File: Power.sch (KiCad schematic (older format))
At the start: 0 parts

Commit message: Added Power Module outline
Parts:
- added C? (x2): C, ~, symbol C
- added F? (x4): FUSE, ~, symbol FUSE
- added L? (x2): INDUCTOR, ~, symbol INDUCTOR
- added P?: CONN_12X2, symbol CONN_12X2
- added R?: R, ~, symbol R
- added SW?: SWITCH_INV, ~, symbol SWITCH_INV
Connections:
- net labels added: +12P, +12V, +3.3V, +5V, -12P, -12V, GND
- wire segments 0 -> 37

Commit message: Fan Current module refactoring
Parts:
- removed F? (x4): FUSE, ~, symbol FUSE
- added TH? (x4): THERMISTOR, ~, symbol THERMISTOR
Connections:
- net labels added: +12C
- wire segments 37 -> 38
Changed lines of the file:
@@
 $Descr A4 11693 8268
 encoding utf-8
-Sheet 5 9
+Sheet 4 9
 Title ""
 Date "4 feb 2014"
@@
 	1    0    0    -1
 $EndComp
-$Comp
-L FUSE F?
-U 1 1 52EFD1CF
-P 3500 2850
-F 0 "F?" H 3600 2900 40  0000 C CNN
-F 1 "FUSE" H 3400 2800 40  0000 C CNN
-F 2 "~" H 3500 2850 60  0000 C CNN
-F 3 "~" H 3500 2850 60  0000 C CNN
-	1    3500 2850
-	1    0    0    -1
-$EndComp
-$Comp
-L FUSE F?
-U 1 1 52EFD1DC
-P 4300 3050
-F 0 "F?" H 4400 3100 40  0000 C CNN
-F 1 "FUSE" H 4200 3000 40  0000 C CNN
-F 2 "~" H 4300 3050 60  0000 C CNN
-F 3 "~" H 4300 3050 60  0000 C CNN
-	1    4300 3050
-	1    0    0    -1
-$EndComp
-$Comp
-L FUSE F?
-U 1 1 52EFD1E2
-P 5050 3250
-F 0 "F?" H 5150 3300 40  0000 C CNN
-F 1 "FUSE" H 4950 3200 40  0000 C CNN
-F 2 "~" H 5050 3250 60  0000 C CNN
-F 3 "~" H 5050 3250 60  0000 C CNN
-	1    5050 3250
-	1    0    0    -1
-$EndComp
-$Comp
-L FUSE F?
-U 1 1 52EFD1E8
-P 5950 3450
-F 0 "F?" H 6050 3500 40  0000 C CNN
-F 1 "FUSE" H 5850 3400 40  0000 C CNN
-F 2 "~" H 5950 3450 60  0000 C CNN
-F 3 "~" H 5950 3450 60  0000 C CNN
-	1    5950 3450
-	1    0    0    -1
-$EndComp
 Wire Wire Line
 	2950 2850 3250 2850
@@
 	9150 5100 9150 5250
 Connection ~ 8700 5100
+Wire Wire Line
+	3200 3250 3200 2400
+Connection ~ 3200 3250
+$Comp
+L +12C #PWR?
+U 1 1 52F156A2
+P 3200 2400
+F 0 "#PWR?" H 3200 2370 30  0001 C CNN
+F 1 "+12C" H 3200 2510 40  0000 C CNN
+F 2 "" H 3200 2400 60  0000 C CNN
+F 3 "" H 3200 2400 60  0000 C CNN
+	1    3200 2400
+	1    0    0    -1
+$EndComp
+$Comp
+L THERMISTOR TH?
+U 1 1 52F1698E
+P 3500 2850
+F 0 "TH?" V 3600 2900 50  0000 C CNN
+F 1 "THERMISTOR" V 3400 2850 50  0000 C CNN
+F 2 "~" H 3500 2850 60  0000 C CNN
+F 3 "~" H 3500 2850 60  0000 C CNN
+	1    3500 2850
+	0    -1   -1   0
+$EndComp
+$Comp
+L THERMISTOR TH?
+U 1 1 52F169A5
+P 4300 3050
+F 0 "TH?" V 4400 3100 50  0000 C CNN
+F 1 "THERMISTOR" V 4200 3050 50  0000 C CNN
+F 2 "~" H 4300 3050 60  0000 C CNN
+F 3 "~" H 4300 3050 60  0000 C CNN
+	1    4300 3050
+	0    -1   -1   0
+$EndComp
+$Comp
+L THERMISTOR TH?
+U 1 1 52F169AB
+P 5050 3250
+F 0 "TH?" V 5150 3300 50  0000 C CNN
+F 1 "THERMISTOR" V 4950 3250 50  0000 C CNN
+F 2 "~" H 5050 3250 60  0000 C CNN
+F 3 "~" H 5050 3250 60  0000 C CNN
+	1    5050 3250
+	0    -1   -1   0
+$EndComp
+$Comp
+L THERMISTOR TH?
+U 1 1 52F169B1
+P 5950 3450
+F 0 "TH?" V 6050 3500 50  0000 C CNN
+F 1 "THERMISTOR" V 5850 3450 50  0000 C CNN
+F 2 "~" H 5950 3450 60  0000 C CNN
+F 3 "~" H 5950 3450 60  0000 C CNN
+	1    5950 3450
+	0    -1   -1   0
+$EndComp
 $EndSCHEMATC

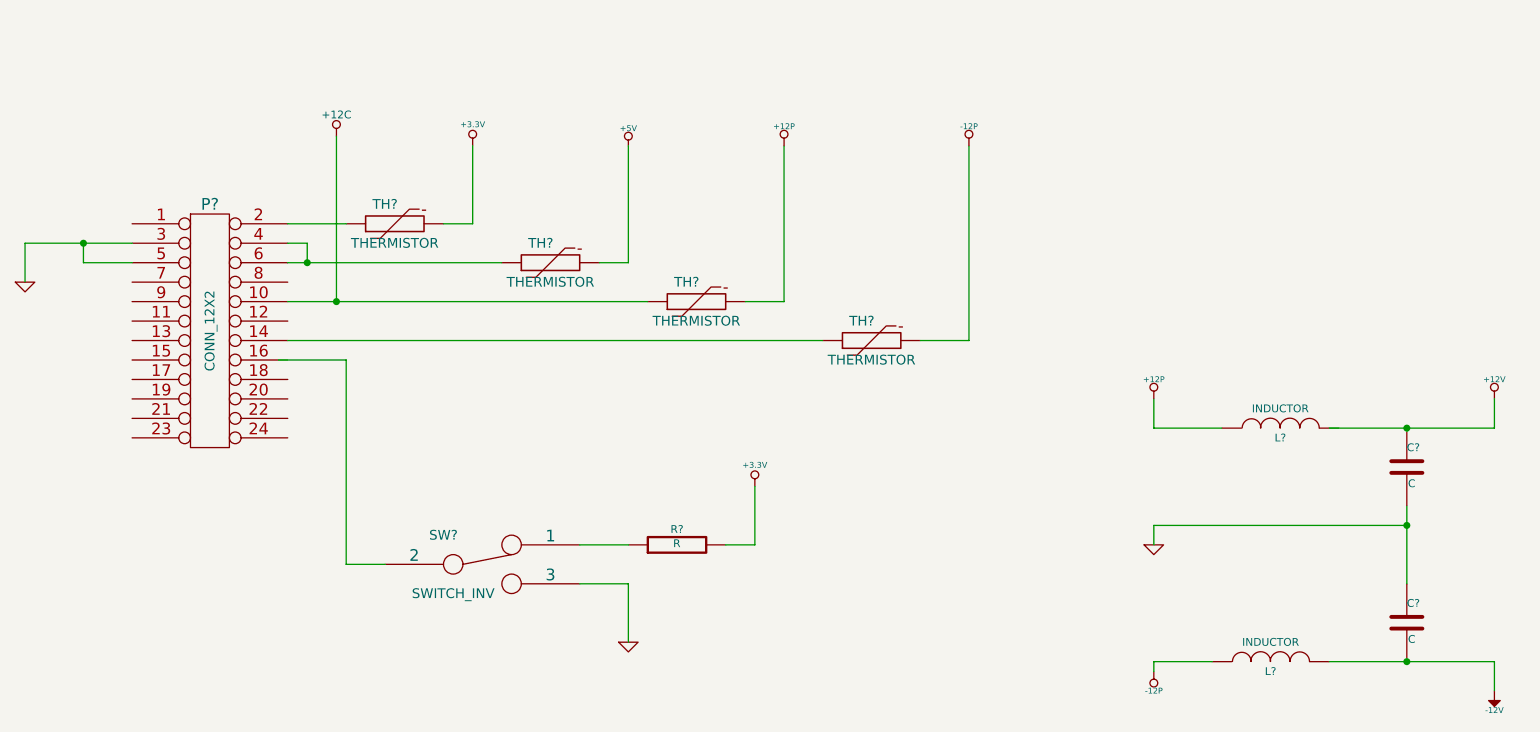
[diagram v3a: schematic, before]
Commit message: Begin Associating relay Module
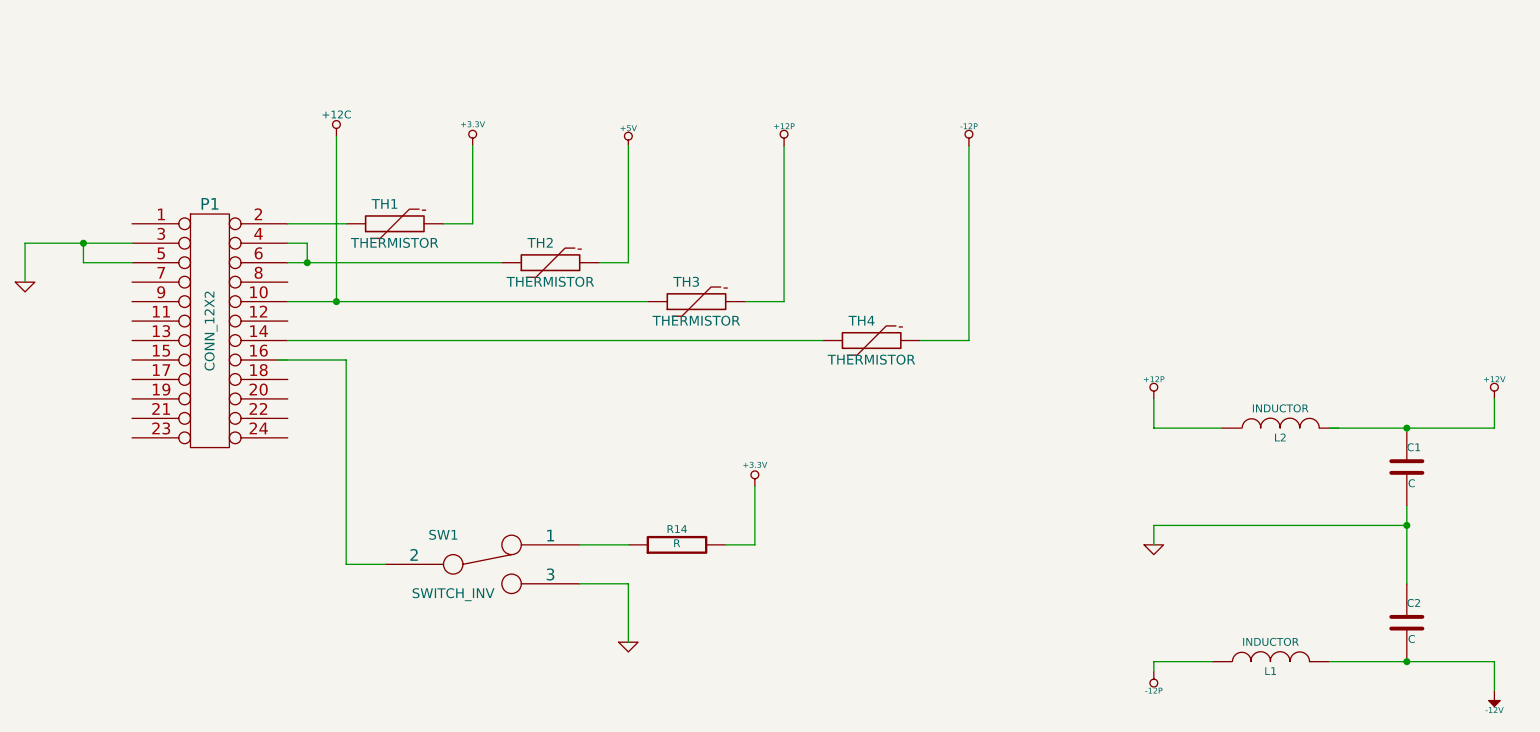
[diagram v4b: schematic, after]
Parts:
- gave numbers to parts that had none: 11
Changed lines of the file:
@@
 LIBS:BenchBudEE
 LIBS:BenchBudEE-cache
-EELAYER 27 0
+EELAYER 24 0
 EELAYER END
 $Descr A4 11693 8268
@@
 $EndDescr
 $Comp
-L CONN_12X2 P?
+L CONN_12X2 P1
 U 1 1 52EFD174
 P 2550 3400
-F 0 "P?" H 2550 4050 60  0000 C CNN
+F 0 "P1" H 2550 4050 60  0000 C CNN
 F 1 "CONN_12X2" V 2550 3400 50  0000 C CNN
 F 2 "" H 2550 3400 60  0000 C CNN
@@
 	1600 2950 1600 3150
 $Comp
-L GND #PWR?
+L GND #PWR13
 U 1 1 52EFD186
 P 1600 3150
-F 0 "#PWR?" H 1600 3150 30  0001 C CNN
+F 0 "#PWR13" H 1600 3150 30  0001 C CNN
 F 1 "GND" H 1600 3080 30  0001 C CNN
 F 2 "" H 1600 3150 60  0000 C CNN
@@
 $EndComp
 $Comp
-L +3.3V #PWR?
+L +3.3V #PWR15
 U 1 1 52EFD19A
 P 3900 2450
-F 0 "#PWR?" H 3900 2410 30  0001 C CNN
+F 0 "#PWR15" H 3900 2410 30  0001 C CNN
 F 1 "+3.3V" H 3900 2560 30  0000 C CNN
 F 2 "" H 3900 2450 60  0000 C CNN
@@
 $EndComp
 $Comp
-L +5V #PWR?
+L +5V #PWR16
 U 1 1 52EFD1B0
 P 4700 2450
-F 0 "#PWR?" H 4700 2540 20  0001 C CNN
+F 0 "#PWR16" H 4700 2540 20  0001 C CNN
 F 1 "+5V" H 4700 2540 30  0000 C CNN
 F 2 "" H 4700 2450 60  0000 C CNN
@@
 	5500 3250 5500 2450
 $Comp
-L +12P #PWR?
+L +12P #PWR19
 U 1 1 52EFD28E
 P 5500 2450
-F 0 "#PWR?" H 5500 2420 30  0001 C CNN
+F 0 "#PWR19" H 5500 2420 30  0001 C CNN
 F 1 "+12P" H 5500 2550 30  0000 C CNN
 F 2 "" H 5500 2450 60  0000 C CNN
@@
 $EndComp
 $Comp
-L -12P #PWR?
+L -12P #PWR20
 U 1 1 52EFD366
 P 6450 2450
-F 0 "#PWR?" H 6450 2420 30  0001 C CNN
+F 0 "#PWR20" H 6450 2420 30  0001 C CNN
 F 1 "-12P" H 6450 2550 30  0000 C CNN
 F 2 "" H 6450 2450 60  0000 C CNN
@@
 Connection ~ 1900 2950
 $Comp
-L SWITCH_INV SW?
+L SWITCH_INV SW1
 U 1 1 52EFD497
 P 3950 4600
-F 0 "SW?" H 3750 4750 50  0000 C CNN
+F 0 "SW1" H 3750 4750 50  0000 C CNN
 F 1 "SWITCH_INV" H 3800 4450 50  0000 C CNN
 F 2 "~" H 3950 4600 60  0000 C CNN
@@
 	4700 4700 4700 5000
 $Comp
-L GND #PWR?
+L GND #PWR17
 U 1 1 52EFD4D4
 P 4700 5000
-F 0 "#PWR?" H 4700 5000 30  0001 C CNN
+F 0 "#PWR17" H 4700 5000 30  0001 C CNN
 F 1 "GND" H 4700 4930 30  0001 C CNN
 F 2 "" H 4700 5000 60  0000 C CNN
@@
 $EndComp
 $Comp
-L R R?
+L R R14
 U 1 1 52EFD4DC
 P 4950 4500
-F 0 "R?" V 5030 4500 40  0000 C CNN
+F 0 "R14" V 5030 4500 40  0000 C CNN
 F 1 "R" V 4957 4501 40  0000 C CNN
 F 2 "~" V 4880 4500 30  0000 C CNN
@@
 	5350 4500 5350 4200
 $Comp
-L +3.3V #PWR?
+L +3.3V #PWR18
 U 1 1 52EFD557
 P 5350 4200
-F 0 "#PWR?" H 5350 4160 30  0001 C CNN
+F 0 "#PWR18" H 5350 4160 30  0001 C CNN
 F 1 "+3.3V" H 5350 4310 30  0000 C CNN
 F 2 "" H 5350 4200 60  0000 C CNN
@@
 $EndComp
 $Comp
-L +12P #PWR?
+L +12P #PWR21
 U 1 1 52EFD66E
 P 7400 3750
-F 0 "#PWR?" H 7400 3720 30  0001 C CNN
+F 0 "#PWR21" H 7400 3720 30  0001 C CNN
 F 1 "+12P" H 7400 3850 30  0000 C CNN
 F 2 "" H 7400 3750 60  0000 C CNN
@@
 $EndComp
 $Comp
-L -12P #PWR?
+L -12P #PWR23
 U 1 1 52EFD674
 P 7400 5150
-F 0 "#PWR?" H 7400 5120 30  0001 C CNN
+F 0 "#PWR23" H 7400 5120 30  0001 C CNN
 F 1 "-12P" H 7400 5250 30  0000 C CNN
 F 2 "" H 7400 5150 60  0000 C CNN
@@
 $EndComp
 $Comp
-L GND #PWR?
+L GND #PWR22
 U 1 1 52EFD67A
 P 7400 4500
-F 0 "#PWR?" H 7400 4500 30  0001 C CNN
+F 0 "#PWR22" H 7400 4500 30  0001 C CNN
 F 1 "GND" H 7400 4430 30  0001 C CNN
 F 2 "" H 7400 4500 60  0000 C CNN
@@
 $EndComp
 $Comp
-L INDUCTOR L?
+L INDUCTOR L2
 U 1 1 52EFD686
 P 8050 3900
-F 0 "L?" V 8000 3900 40  0000 C CNN
+F 0 "L2" V 8000 3900 40  0000 C CNN
 F 1 "INDUCTOR" V 8150 3900 40  0000 C CNN
 F 2 "~" H 8050 3900 60  0000 C CNN
@@
 $EndComp
 $Comp
-L INDUCTOR L?
+L INDUCTOR L1
 U 1 1 52EFD693
 P 8000 5100
-F 0 "L?" V 7950 5100 40  0000 C CNN
+F 0 "L1" V 7950 5100 40  0000 C CNN
 F 1 "INDUCTOR" V 8100 5100 40  0000 C CNN
 F 2 "~" H 8000 5100 60  0000 C CNN
@@
 $EndComp
 $Comp
-L C C?
+L C C1
 U 1 1 52EFD69B
 P 8700 4100
-F 0 "C?" H 8700 4200 40  0000 L CNN
+F 0 "C1" H 8700 4200 40  0000 L CNN
 F 1 "C" H 8706 4015 40  0000 L CNN
 F 2 "~" H 8738 3950 30  0000 C CNN
@@
 $EndComp
 $Comp
-L C C?
+L C C2
 U 1 1 52EFD6A8
 P 8700 4900
-F 0 "C?" H 8700 5000 40  0000 L CNN
+F 0 "C2" H 8700 5000 40  0000 L CNN
 F 1 "C" H 8706 4815 40  0000 L CNN
 F 2 "~" H 8738 4750 30  0000 C CNN
@@
 Connection ~ 8700 4400
 $Comp
-L +12V #PWR?
+L +12V #PWR24
 U 1 1 52EFD773
 P 9150 3750
-F 0 "#PWR?" H 9150 3700 20  0001 C CNN
+F 0 "#PWR24" H 9150 3700 20  0001 C CNN
 F 1 "+12V" H 9150 3850 30  0000 C CNN
 F 2 "" H 9150 3750 60  0000 C CNN
@@
 	7400 5100 7700 5100
 $Comp
-L -12V #PWR?
+L -12V #PWR25
 U 1 1 52EFD7D2
 P 9150 5250
-F 0 "#PWR?" H 9150 5380 20  0001 C CNN
+F 0 "#PWR25" H 9150 5380 20  0001 C CNN
 F 1 "-12V" H 9150 5350 30  0000 C CNN
 F 2 "" H 9150 5250 60  0000 C CNN
@@
 Connection ~ 3200 3250
 $Comp
-L +12C #PWR?
+L +12C #PWR14
 U 1 1 52F156A2
 P 3200 2400
-F 0 "#PWR?" H 3200 2370 30  0001 C CNN
+F 0 "#PWR14" H 3200 2370 30  0001 C CNN
 F 1 "+12C" H 3200 2510 40  0000 C CNN
 F 2 "" H 3200 2400 60  0000 C CNN
@@
 $EndComp
 $Comp
-L THERMISTOR TH?
+L THERMISTOR TH1
 U 1 1 52F1698E
 P 3500 2850
-F 0 "TH?" V 3600 2900 50  0000 C CNN
+F 0 "TH1" V 3600 2900 50  0000 C CNN
 F 1 "THERMISTOR" V 3400 2850 50  0000 C CNN
 F 2 "~" H 3500 2850 60  0000 C CNN
@@
 $EndComp
 $Comp
-L THERMISTOR TH?
+L THERMISTOR TH2
 U 1 1 52F169A5
 P 4300 3050
-F 0 "TH?" V 4400 3100 50  0000 C CNN
+F 0 "TH2" V 4400 3100 50  0000 C CNN
 F 1 "THERMISTOR" V 4200 3050 50  0000 C CNN
 F 2 "~" H 4300 3050 60  0000 C CNN
@@
 $EndComp
 $Comp
-L THERMISTOR TH?
+L THERMISTOR TH3
 U 1 1 52F169AB
 P 5050 3250
-F 0 "TH?" V 5150 3300 50  0000 C CNN
+F 0 "TH3" V 5150 3300 50  0000 C CNN
 F 1 "THERMISTOR" V 4950 3250 50  0000 C CNN
 F 2 "~" H 5050 3250 60  0000 C CNN
@@
 $EndComp
 $Comp
-L THERMISTOR TH?
+L THERMISTOR TH4
 U 1 1 52F169B1
 P 5950 3450
-F 0 "TH?" V 6050 3500 50  0000 C CNN
+F 0 "TH4" V 6050 3500 50  0000 C CNN
 F 1 "THERMISTOR" V 5850 3450 50  0000 C CNN
 F 2 "~" H 5950 3450 60  0000 C CNN

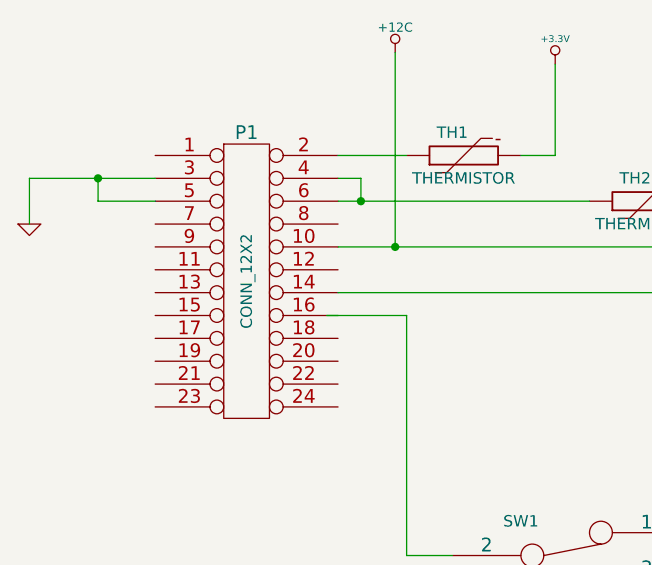
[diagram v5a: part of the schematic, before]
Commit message: Placement of connectors
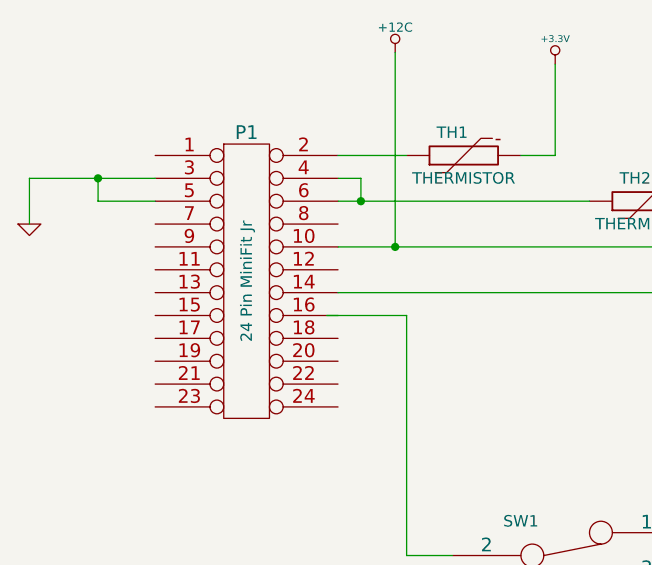
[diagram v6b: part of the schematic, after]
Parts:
- P1: value CONN_12X2 -> 24 Pin MiniFit Jr; MFG Name (none) -> Molex; MFG Part Number (none) -> 39-30-1240
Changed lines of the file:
@@
 P 2550 3400
 F 0 "P1" H 2550 4050 60  0000 C CNN
-F 1 "CONN_12X2" V 2550 3400 50  0000 C CNN
+F 1 "24 Pin MiniFit Jr" V 2550 3400 50  0000 C CNN
 F 2 "" H 2550 3400 60  0000 C CNN
 F 3 "" H 2550 3400 60  0000 C CNN
+F 4 "Molex" H 2550 3400 60  0001 C CNN "MFG Name"
+F 5 "39-30-1240" H 2550 3400 60  0001 C CNN "MFG Part Number"
 	1    2550 3400
 	1    0    0    -1
@@
 	1600 2950 1600 3150
 $Comp
-L GND #PWR018
+L GND #PWR18
 U 1 1 52EFD186
 P 1600 3150
-F 0 "#PWR018" H 1600 3150 30  0001 C CNN
+F 0 "#PWR18" H 1600 3150 30  0001 C CNN
 F 1 "GND" H 1600 3080 30  0001 C CNN
 F 2 "" H 1600 3150 60  0000 C CNN
@@
 $EndComp
 $Comp
-L +3.3V #PWR019
+L +3.3V #PWR20
 U 1 1 52EFD19A
 P 3900 2450
-F 0 "#PWR019" H 3900 2410 30  0001 C CNN
+F 0 "#PWR20" H 3900 2410 30  0001 C CNN
 F 1 "+3.3V" H 3900 2560 30  0000 C CNN
 F 2 "" H 3900 2450 60  0000 C CNN
@@
 $EndComp
 $Comp
-L +5V #PWR020
+L +5V #PWR21
 U 1 1 52EFD1B0
 P 4700 2450
-F 0 "#PWR020" H 4700 2540 20  0001 C CNN
+F 0 "#PWR21" H 4700 2540 20  0001 C CNN
 F 1 "+5V" H 4700 2540 30  0000 C CNN
 F 2 "" H 4700 2450 60  0000 C CNN
@@
 	5500 3250 5500 2450
 $Comp
-L +12P #PWR021
+L +12P #PWR24
 U 1 1 52EFD28E
 P 5500 2450
-F 0 "#PWR021" H 5500 2420 30  0001 C CNN
+F 0 "#PWR24" H 5500 2420 30  0001 C CNN
 F 1 "+12P" H 5500 2550 30  0000 C CNN
 F 2 "" H 5500 2450 60  0000 C CNN
@@
 $EndComp
 $Comp
-L -12P #PWR022
+L -12P #PWR25
 U 1 1 52EFD366
 P 6450 2450
-F 0 "#PWR022" H 6450 2420 30  0001 C CNN
+F 0 "#PWR25" H 6450 2420 30  0001 C CNN
 F 1 "-12P" H 6450 2550 30  0000 C CNN
 F 2 "" H 6450 2450 60  0000 C CNN
@@
 	4700 4700 4700 5000
 $Comp
-L GND #PWR023
+L GND #PWR22
 U 1 1 52EFD4D4
 P 4700 5000
-F 0 "#PWR023" H 4700 5000 30  0001 C CNN
+F 0 "#PWR22" H 4700 5000 30  0001 C CNN
 F 1 "GND" H 4700 4930 30  0001 C CNN
 F 2 "" H 4700 5000 60  0000 C CNN
@@
 	5350 4500 5350 4200
 $Comp
-L +3.3V #PWR024
+L +3.3V #PWR23
 U 1 1 52EFD557
 P 5350 4200
-F 0 "#PWR024" H 5350 4160 30  0001 C CNN
+F 0 "#PWR23" H 5350 4160 30  0001 C CNN
 F 1 "+3.3V" H 5350 4310 30  0000 C CNN
 F 2 "" H 5350 4200 60  0000 C CNN
@@
 $EndComp
 $Comp
-L +12P #PWR025
+L +12P #PWR26
 U 1 1 52EFD66E
 P 7400 3750
-F 0 "#PWR025" H 7400 3720 30  0001 C CNN
+F 0 "#PWR26" H 7400 3720 30  0001 C CNN
 F 1 "+12P" H 7400 3850 30  0000 C CNN
 F 2 "" H 7400 3750 60  0000 C CNN
@@
 $EndComp
 $Comp
-L -12P #PWR026
+L -12P #PWR28
 U 1 1 52EFD674
 P 7400 5150
-F 0 "#PWR026" H 7400 5120 30  0001 C CNN
+F 0 "#PWR28" H 7400 5120 30  0001 C CNN
 F 1 "-12P" H 7400 5250 30  0000 C CNN
 F 2 "" H 7400 5150 60  0000 C CNN
@@
 $EndComp
 $Comp
-L GND #PWR027
+L GND #PWR27
 U 1 1 52EFD67A
 P 7400 4500
-F 0 "#PWR027" H 7400 4500 30  0001 C CNN
+F 0 "#PWR27" H 7400 4500 30  0001 C CNN
 F 1 "GND" H 7400 4430 30  0001 C CNN
 F 2 "" H 7400 4500 60  0000 C CNN
@@
 Connection ~ 8700 4400
 $Comp
-L +12V #PWR028
+L +12V #PWR29
 U 1 1 52EFD773
 P 9150 3750
-F 0 "#PWR028" H 9150 3700 20  0001 C CNN
+F 0 "#PWR29" H 9150 3700 20  0001 C CNN
 F 1 "+12V" H 9150 3850 30  0000 C CNN
 F 2 "" H 9150 3750 60  0000 C CNN
@@
 	7400 5100 7700 5100
 $Comp
-L -12V #PWR029
+L -12V #PWR30
 U 1 1 52EFD7D2
 P 9150 5250
-F 0 "#PWR029" H 9150 5380 20  0001 C CNN
+F 0 "#PWR30" H 9150 5380 20  0001 C CNN
 F 1 "-12V" H 9150 5350 30  0000 C CNN
 F 2 "" H 9150 5250 60  0000 C CNN
@@
 Connection ~ 3200 3250
 $Comp
-L +12C #PWR030
+L +12C #PWR19
 U 1 1 52F156A2
 P 3200 2400
-F 0 "#PWR030" H 3200 2370 30  0001 C CNN
+F 0 "#PWR19" H 3200 2370 30  0001 C CNN
 F 1 "+12C" H 3200 2510 40  0000 C CNN
 F 2 "" H 3200 2400 60  0000 C CNN
